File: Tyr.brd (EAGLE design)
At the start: 152.4 x 115.6 mm, 210 parts, among them J1 TYR_TYR_DISPLAY, Q1 DTC123J, SW1 BUTTON, SW10 KEYBOARD_KEYSWITCH-MX-1U-HOTS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, SW11 KEYBOARD_KEYSWITCH-MX-1U-HOTS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, SW12 KEYBOARD_KEYSWITCH-MX-1U-HOTS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, SW13 KEYBOARD_KEYSWITCH-MX-1U-HOTS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, SW14 KEYBOARD_KEYSWITCH-MX-1U-HOTS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, SW15 KEYBOARD_KEYSWITCH-MX-1U-HOTS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, SW16 KEYBOARD_KEYSWITCH-MX-1U-HOTS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, SW17 KEYBOARD_KEYSWITCH-MX-1U-HOTS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, SW18 KEYBOARD_KEYSWITCH-MX-1U-HOTS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, SW19 KEYBOARD_KEYSWITCH-MX-1U-HOTS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, SW2 KEYBOARD_KEYSWITCH-MX-1U-HOTS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, SW20 KEYBOARD_KEYSWITCH-MX-1U-HOTS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, SW21 KEYBOARD_KEYSWITCH-MX-1U-HOTS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, SW22 KEYBOARD_KEYSWITCH-MX-1U-HOTS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, SW23 KEYBOARD_KEYSWITCH-MX-1U-HOTS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, SW24 KEYBOARD_KEYSWITCH-MX-1U-HOTS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, SW25 KEYBOARD_KEYSWITCH-MX-1U-HOTS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, SW26 KEYBOARD_KEYSWITCH-MX-1U-HOTS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, SW27 KEYBOARD_KEYSWITCH-MX-1U-HOTS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, SW28 KEYBOARD_KEYSWITCH-MX-1U-HOTS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, SW29 KEYBOARD_KEYSWITCH-MX-1U-HOTS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, SW3 KEYBOARD_KEYSWITCH-MX-1U-HOTS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, SW30 KEYBOARD_KEYSWITCH-MX-1U-HOTS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, SW31 KEYBOARD_KEYSWITCH-MX-1U-HOTS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, SW32 KEYBOARD_KEYSWITCH-MX-2U-HOTS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, SW33 KEYBOARD_KEYSWITCH-MX-1U-HOTS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, SW34 KEYBOARD_KEYSWITCH-MX-1U-HOTS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, SW35 KEYBOARD_KEYSWITCH-MX-1U-HOTS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, SW36 KEYBOARD_KEYSWITCH-MX-1U-HOTS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, SW37 KEYBOARD_KEYSWITCH-MX-1U-HOTS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, SW38 KEYBOARD_KEYSWITCH-MX-1U-HOTS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, SW39 KEYBOARD_KEYSWITCH-MX-1U-HOTS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, SW4 KEYBOARD_KEYSWITCH-MX-1U-HOTS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, SW40 KEYBOARD_KEYSWITCH-MX-1U-HOTS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, SW41 KEYBOARD_KEYSWITCH-MX-2U-HOTS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, SW42 KEYBOARD_KEYSWITCH-MX-1U-HOTS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, SW5 KEYBOARD_KEYSWITCH-MX-1U-HOTS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, SW6 KEYBOARD_KEYSWITCH-MX-1U-HOTS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, SW7 KEYBOARD_KEYSWITCH-MX-1U-HOTS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, SW8 KEYBOARD_KEYSWITCH-MX-1U-HOTS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, SW9 KEYBOARD_KEYSWITCH-MX-1U-HOTS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, U1 MCP1700T, U2 CONTROLLER_PRTR5V0U2X, U3 STM32F303CC, U4 MB85RC256V, U6 TYR_TPS2552, X1 CONTROLLER_USB-C-12PUSB-C-12P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, Y1 8Mhz

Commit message: Update library
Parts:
- C1, C10, C11, C12, C13, C14, C15, C16, C17, C18, C19, C2, C20, C21, C22, C23, C24, C25, C26, C27, C28, C29, C3, C30, C31, C32, C33, C34, C35, C36, C37, C38, C39, C4, C40, C41, C42, C43, C44, C45, C46, C47, C48, C49, C5, C50, C51, C52, C6, C7, C8, C9: device Tyr:COMPONENTS_C0603 -> Tyr:C0603
- D1, D10, D11, D12, D13, D14, D15, D16, D17, D18, D19, D2, D20, D21, D22, D23, D24, D25, D26, D27, D28, D29, D3, D30, D31, D32, D33, D34, D35, D36, D37, D38, D39, D4, D40, D41, D42, D43, D44, D5, D6, D7, D8, D9: device Tyr:COMPONENTS_SOD-123 -> Tyr:SOD-123
- HOLE1, HOLE2: value HOLE_MOUNT_HOLE5MM_NOTCH -> MOUNT_HOLE5MM_NOTCH
- HOLE3, HOLE4, HOLE5, HOLE6: value HOLE_MOUNT_HOLE -> MOUNT_HOLE
- J1: value TYR_TYR_DISPLAY -> TYR_DISPLAY
- LED1, LED10, LED11, LED12, LED13, LED14, LED15, LED16, LED17, LED18, LED19, LED2, LED20, LED21, LED22, LED23, LED24, LED25, LED26, LED27, LED28, LED29, LED3, LED30, LED31, LED32, LED33, LED34, LED35, LED36, LED37, LED38, LED39, LED4, LED40, LED41, LED5, LED6, LED7, LED8, LED9: value TYR_WS2812B_3528_REVERS-MOUNT -> WS2812B_3528_REVERS-MOUNT; device Tyr:TYR_WS2812B_3528_REVERS-MOUNT -> Tyr:WS2812B_3528_REVERS-MOUNT
- R1, R11, R12, R2, R3, R4, R5, R6, R7, R8, R9: device Tyr:COMPONENTS_R0603 -> Tyr:R0603
- R10: device Tyr:MICROBUILDER_2512 -> Tyr:R2512
- SJ1: device Tyr:MICROBUILDER_SOLDERJUMPER_ARROW_NOPASTE -> Tyr:SOLDERJUMPER_ARROW_NOPASTE
- SW10, SW11, SW12, SW13, SW14, SW15, SW16, SW17, SW18, SW19, SW2, SW20, SW21, SW22, SW23, SW24, SW26, SW27, SW28, SW29, SW3, SW30, SW31, SW33, SW34, SW35, SW36, SW37, SW38, SW39, SW4, SW40, SW42, SW5, SW6, SW7, SW8, SW9: value KEYBOARD_KEYSWITCH-MX-1U-HOTSWAP -> KEYSWITCH-MX-1U-HOTSWAP; device Tyr:KEYBOARD_MX-1U-HOTSWAP -> Tyr:MX-1U-HOTSWAP
- SW25: value KEYBOARD_KEYSWITCH-MX-1U-HOTSWAPCAPSLOCK -> KEYSWITCH-MX-1U-HOTSWAPCAPSLOCK; device Tyr:KEYBOARD_MX-1U-HOTSWAP-CAPSLOCK -> Tyr:MX-1U-HOTSWAP-CAPSLOCK
- SW32, SW41: value KEYBOARD_KEYSWITCH-MX-2U-HOTSWAP -> KEYSWITCH-MX-2U-HOTSWAP; device Tyr:KEYBOARD_MX-2U-HOTSWAP -> Tyr:MX-2U-HOTSWAP
- U2: value CONTROLLER_PRTR5V0U2X -> PRTR5V0U2X; device Tyr:CONTROLLER_PRTR5V0U2X -> Tyr:PRTR5V0U2X
- U5: device Tyr:MICROBUILDER_SOT23-8 -> Tyr:SOT23-8
- U6: value TYR_TPS2552 -> TPS2552; device Tyr:TYR_SOT-23-6P -> Tyr:SOT-23-6P
- X1: value CONTROLLER_USB-C-12PUSB-C-12P-INBOARD -> USB-C-12P-INBOARD; device Tyr:CONTROLLER_USB-C-12P-INBOARD -> Tyr:USB-C-12P-INBOARD
- Y1: device Tyr:CONTROLLER_CRYSTAL-3.2X2.5 -> Tyr:CRYSTAL-3.2X2.5

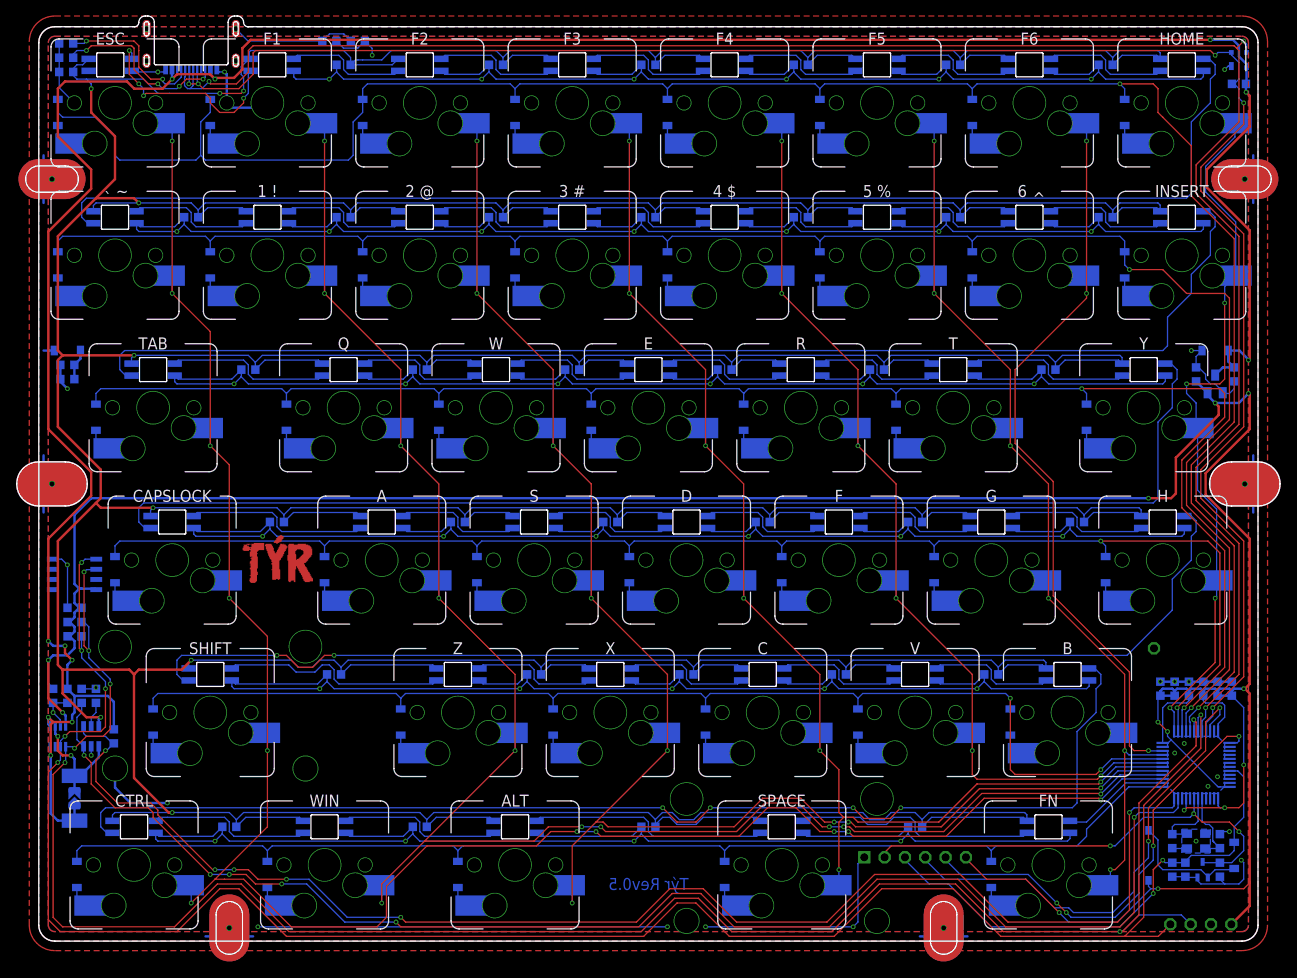
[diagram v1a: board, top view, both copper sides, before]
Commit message: Remove bottom outer ring
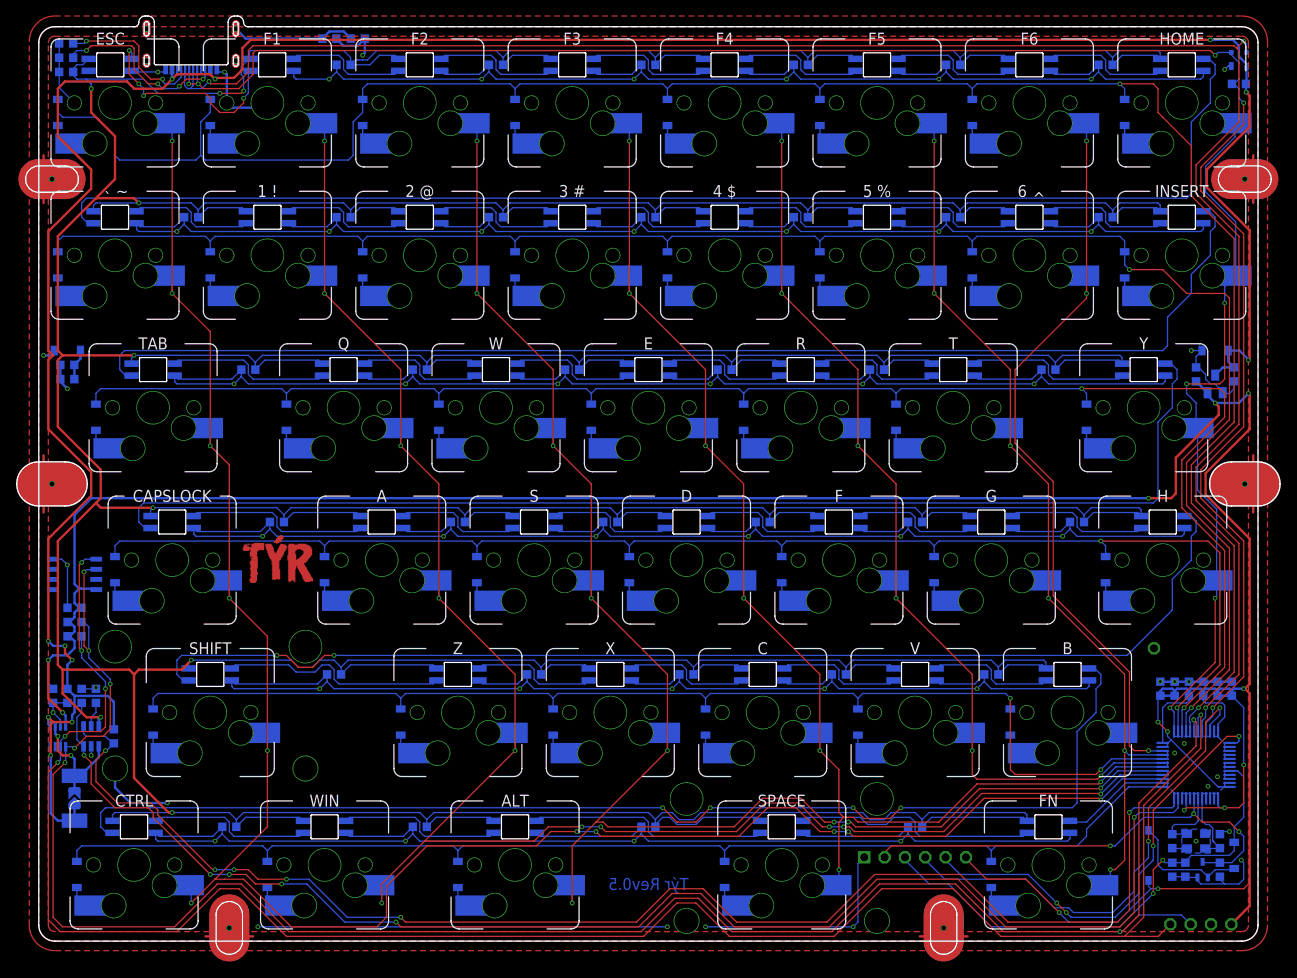
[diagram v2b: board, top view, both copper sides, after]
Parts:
- moved C12 0.30 mm to (39.9, 112.8)
- moved R4 0.30 mm to (36.3, 112.8)
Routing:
- net CASE: track 44.7 -> 44.9 mm, vias 0 -> 1
- removed copper zone on layer 16, net CASE

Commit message: Update
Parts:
- SW10, SW11, SW12, SW13, SW14, SW15, SW16, SW17, SW18, SW19, SW2, SW20, SW21, SW22, SW23, SW24, SW26, SW27, SW28, SW29, SW3, SW30, SW31, SW33, SW34, SW35, SW36, SW37, SW38, SW39, SW4, SW40, SW42, SW5, SW6, SW7, SW8, SW9: value KEYSWITCH-MX-1U-HOTSWAP -> KEYSWITCH-MX_PLATED-1U-HOTSWAP
- SW25: value KEYSWITCH-MX-1U-HOTSWAPCAPSLOCK -> KEYSWITCH-MX_PLATED-1U-HOTSWAP_CAPSLOCK
- SW32, SW41: value KEYSWITCH-MX-2U-HOTSWAP -> KEYSWITCH-MX_PLATED-2U-HOTSWAP
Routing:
- net CASE: track 44.9 -> 19.5 mm

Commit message: Update
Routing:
- net GND: track 1211.2 -> 1215.1 mm, vias 59 -> 60
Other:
- board text removed: "JLCJLCJLC JLCJLCJLC"
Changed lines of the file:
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@@
 <drawing>
 <settings>
-<setting alwaysvectorfont="no"/>
+<setting alwaysvectorfont="yes"/>
 <setting verticaltext="up"/>
 </settings>
@@
 <wire x1="2" y1="0" x2="150.4" y2="0" width="0" layer="20"/>
 <wire x1="150.4" y1="0" x2="152.4" y2="2" width="0" layer="20" curve="90"/>
-<text x="13.98984375" y="4.099609375" size="0.8" layer="22" font="vector" rot="MR0" align="center">JLCJLCJLC
-JLCJLCJLC</text>
 <wire x1="12.5015625" y1="114.839453125" x2="11.962109375" y2="114.3" width="0.001" layer="20" curve="-90"/>
 <wire x1="11.962109375" y1="114.3" x2="11.90625" y2="114.3" width="0.001" layer="20"/>
@@
 <contactref element="X1" pad="GND2"/>
 <contactref element="U2" pad="1"/>
-<contactref element="J1" pad="GND"/>
 <contactref element="U6" pad="2"/>
 <contactref element="C15" pad="1"/>
@@
 <wire x1="40.7609375" y1="112.81171875" x2="40.7609375" y2="111.0078125" width="0.3048" layer="16"/>
 <wire x1="40.7609375" y1="111.0078125" x2="40.48125" y2="110.728125" width="0.3048" layer="16"/>
+<contactref element="J1" pad="GND"/>
+<wire x1="149.06625" y1="2.1" x2="150.6140625" y2="3.6478125" width="0.3048" layer="16"/>
+<wire x1="150.6140625" y1="3.6478125" x2="150.6140625" y2="5.3578125" width="0.3048" layer="16"/>
+<via x="150.6140625" y="5.3578125" extent="1-16" drill="0.35"/>
 </signal>
 <signal name="VCC">
@@
 <wire x1="145.8515625" y1="58.489453125" x2="145.8515625" y2="55.810546875" width="0.3048" layer="1"/>
 <wire x1="151.358203125" y1="50.30390625" x2="145.8515625" y2="55.810546875" width="0.3048" layer="1"/>
-<contactref element="J1" pad="VIN"/>
-<wire x1="151.358203125" y1="4.391953125" x2="151.358203125" y2="7.292578125" width="0.3048" layer="1"/>
-<wire x1="151.358203125" y1="4.391953125" x2="149.06625" y2="2.1" width="0.3048" layer="1"/>
 <via x="139.8984375" y="6.5484375" extent="1-16" drill="0.35"/>
-<wire x1="139.8984375" y1="6.5484375" x2="150.6140625" y2="6.5484375" width="0.1524" layer="1"/>
 <contactref element="SW1" pad="P$2"/>
-<wire x1="151.358203125" y1="7.292578125" x2="150.6140625" y2="6.5484375" width="0.1524" layer="1"/>
 <wire x1="139.8984375" y1="6.5484375" x2="139.005078125" y2="6.5484375" width="0.1524" layer="16"/>
 <contactref element="PH1" pad="6"/>
@@
 <wire x1="141.0890625" y1="29.765625" x2="140.4826375" y2="29.1592" width="0.1524" layer="16"/>
 <wire x1="148.2328125" y1="27.9796875" x2="148.2328125" y2="29.46796875" width="0.1524" layer="16"/>
-<wire x1="148.8392375" y1="19.2765625" x2="147.6375" y2="19.2765625" width="0.1524" layer="16"/>
-<wire x1="147.4109375" y1="19.2765625" x2="147.6375" y2="19.2765625" width="0.1524" layer="16"/>
+<wire x1="148.8392375" y1="19.2765625" x2="147.4109375" y2="19.2765625" width="0.1524" layer="16"/>
 <wire x1="140.19609375" y1="30.6765625" x2="139.8984375" y2="30.37890625" width="0.1524" layer="16"/>
 <wire x1="139.8984375" y1="30.37890625" x2="139.8984375" y2="27.384375" width="0.1524" layer="16"/>
@@
 <wire x1="1.190625" y1="30.3609375" x2="2.9765625" y2="28.575" width="0.3048" layer="1"/>
 <wire x1="151.358203125" y1="50.30390625" x2="151.358203125" y2="32.146875" width="0.3048" layer="1"/>
-<wire x1="151.358203125" y1="30.95625" x2="151.358203125" y2="7.292578125" width="0.3048" layer="1"/>
+<wire x1="151.358203125" y1="30.95625" x2="151.358203125" y2="7.14375" width="0.3048" layer="1"/>
+<wire x1="151.358203125" y1="7.14375" x2="151.358203125" y2="4.911328125" width="0.3048" layer="1"/>
 <wire x1="118.4671875" y1="7.7390625" x2="115.8875" y2="10.31875" width="0.1524" layer="1"/>
 <wire x1="115.8875" y1="10.31875" x2="115.8875" y2="10.4775" width="0.1524" layer="1"/>
@@
 <via x="141.0890625" y="26.19375" extent="1-16" drill="0.35"/>
 <wire x1="141.0890625" y1="25.5984375" x2="141.0890625" y2="26.19375" width="0.1524" layer="16"/>
-<wire x1="147.4109375" y1="19.2765625" x2="147.33984375" y2="19.34765625" width="0.1524" layer="16"/>
-<wire x1="141.0890625" y1="25.5984375" x2="147.33984375" y2="19.34765625" width="0.1524" layer="16"/>
+<wire x1="141.0890625" y1="25.5984375" x2="147.4109375" y2="19.2765625" width="0.1524" layer="16"/>
 <wire x1="149.4234375" y1="31.5515625" x2="150.6140625" y2="31.5515625" width="0.3048" layer="16"/>
 <via x="150.6140625" y="31.5515625" extent="1-16" drill="0.35"/>
@@
 <wire x1="151.358203125" y1="30.95625" x2="150.762890625" y2="31.5515625" width="0.3048" layer="1"/>
 <wire x1="150.762890625" y1="31.5515625" x2="150.6140625" y2="31.5515625" width="0.3048" layer="1"/>
-<wire x1="3.58984375" y1="38.1" x2="3.86953125" y2="38.1" width="0.3048" layer="16"/>
-<wire x1="3.58984375" y1="39.8859375" x2="3.86953125" y2="39.8859375" width="0.3048" layer="16"/>
-<wire x1="5.06015625" y1="41.671875" x2="5.33984375" y2="41.671875" width="0.3048" layer="16"/>
 <wire x1="146.0921875" y1="68.5515625" x2="146.0921875" y2="68.2203125" width="0.3048" layer="16"/>
 <wire x1="146.0921875" y1="68.2203125" x2="147.0421875" y2="67.2703125" width="0.3048" layer="16"/>
@@
 <wire x1="4.46484375" y1="43.4578125" x2="4.46484375" y2="42.2671875" width="0.3048" layer="16"/>
 <wire x1="4.46484375" y1="42.2671875" x2="5.06015625" y2="41.671875" width="0.3048" layer="16"/>
-<wire x1="5.06015625" y1="41.671875" x2="5.33984375" y2="41.671875" width="0.3048" layer="16"/>
 <wire x1="6.5484375" y1="55.3640625" x2="4.46484375" y2="53.28046875" width="0.3048" layer="16"/>
 <wire x1="4.46484375" y1="37.5046875" x2="3.86953125" y2="38.1" width="0.3048" layer="16"/>
-<wire x1="3.86953125" y1="38.1" x2="3.58984375" y2="38.1" width="0.3048" layer="16"/>
 <wire x1="3.571875" y1="35.71875" x2="4.46484375" y2="36.61171875" width="0.3048" layer="16"/>
 <wire x1="4.46484375" y1="36.61171875" x2="4.46484375" y2="37.5046875" width="0.3048" layer="16"/>
-<wire x1="3.58984375" y1="39.8859375" x2="3.86953125" y2="39.8859375" width="0.3048" layer="16"/>
 <wire x1="4.46484375" y1="39.290625" x2="3.86953125" y2="39.8859375" width="0.3048" layer="16"/>
 <wire x1="3.58984375" y1="39.8859375" x2="3.86953125" y2="39.8859375" width="0.3048" layer="16"/>
@@
 <wire x1="7.17984375" y1="43.9340625" x2="7.06078125" y2="44.053125" width="0.3048" layer="16"/>
 <wire x1="5.06015625" y1="44.053125" x2="4.46484375" y2="44.6484375" width="0.3048" layer="16"/>
-<wire x1="7.06078125" y1="44.053125" x2="5.3578125" y2="44.053125" width="0.3048" layer="16"/>
-<wire x1="5.3578125" y1="44.053125" x2="5.06015625" y2="44.053125" width="0.3048" layer="16"/>
-<wire x1="5.3578125" y1="44.053125" x2="5.06015625" y2="44.053125" width="0.3048" layer="16"/>
+<wire x1="7.06078125" y1="44.053125" x2="5.06015625" y2="44.053125" width="0.3048" layer="16"/>
 <wire x1="5.06015625" y1="44.053125" x2="4.46484375" y2="43.4578125" width="0.3048" layer="16"/>
+<contactref element="J1" pad="VIN"/>
+<wire x1="146.52625" y1="2.1" x2="147.998125" y2="3.571875" width="0.3048" layer="1"/>
+<wire x1="147.998125" y1="3.571875" x2="150.01875" y2="3.571875" width="0.3048" layer="1"/>
+<wire x1="150.01875" y1="3.571875" x2="151.358203125" y2="4.911328125" width="0.3048" layer="1"/>
+<wire x1="150.762890625" y1="6.5484375" x2="151.358203125" y2="7.14375" width="0.1524" layer="1"/>
+<wire x1="139.8984375" y1="6.5484375" x2="150.01875" y2="6.5484375" width="0.1524" layer="1"/>
+<wire x1="150.01875" y1="6.5484375" x2="150.762890625" y2="6.5484375" width="0.1524" layer="1"/>
 </signal>
 <signal name="NRST">
@@
 </drawing>
 <compatibility>
-<note version="6.3" minversion="6.2.2" severity="warning">
-Since Version 6.2.2 text objects can contain more than one line,
-which will not be processed correctly with this version.
-</note>
 <note version="8.2" severity="warning">
 Since Version 8.2, EAGLE supports online libraries. The ids

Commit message: Rev0.5
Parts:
- C18, C19, C20, C21, C22, C23, C24, C25, C26, C27, C28, C29, C30, C31, C32, C33, C34, C35, C36, C37, C38, C39, C40, C41, C42, C43, C44, C45, C46, C47, C48, C49, C50, C51, C52: value 104 -> 100n
- HOLE1, HOLE2: value MOUNT_HOLE5MM_NOTCH -> MOUNT_HOLE-5MM_NOTCH
- SW10, SW11, SW12, SW13, SW14, SW15, SW16, SW17, SW18, SW19, SW2, SW20, SW21, SW22, SW23, SW24, SW26, SW27, SW28, SW29, SW3, SW30, SW31, SW33, SW34, SW35, SW36, SW37, SW38, SW39, SW4, SW40, SW42, SW5, SW6, SW7, SW8, SW9: value KEYSWITCH-MX_PLATED-1U-HOTSWAP -> MX
- SW25: value KEYSWITCH-MX_PLATED-1U-HOTSWAP_CAPSLOCK -> MX
- SW32, SW41: value KEYSWITCH-MX_PLATED-2U-HOTSWAP -> MX
